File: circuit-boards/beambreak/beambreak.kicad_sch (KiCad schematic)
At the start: 12 parts, among them J1 POWER, J2 SENSOR, J3 RRIB, U1 H11L1SM

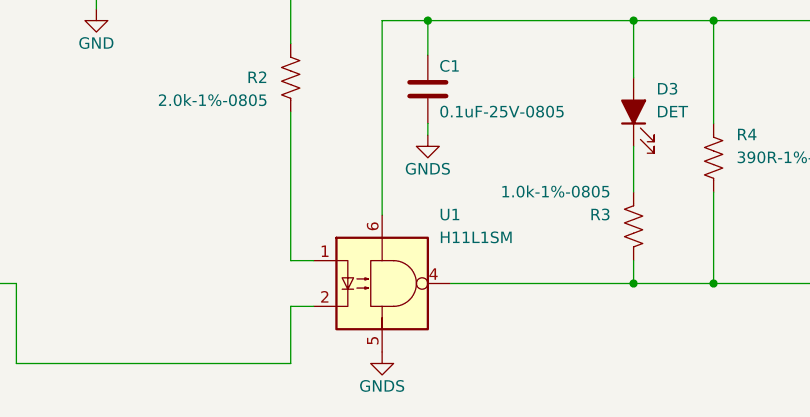
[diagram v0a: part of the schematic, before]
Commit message: Fixing bom and created gerbers for beam break board
Signed-off-by: Scott Berman <sgberman1@gmail.com>
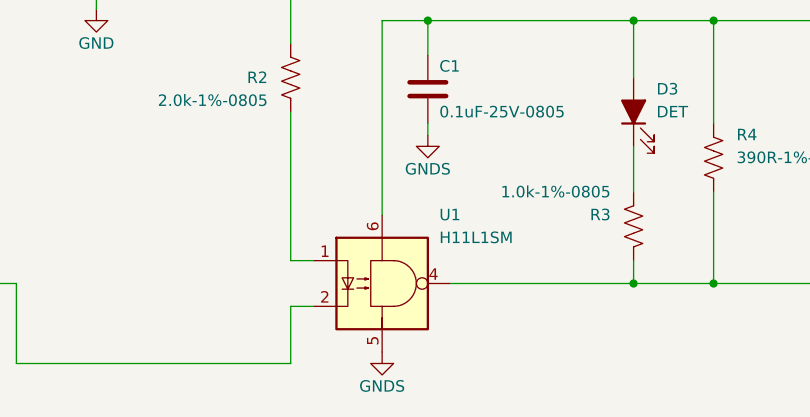
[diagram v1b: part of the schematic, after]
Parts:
- C1: DIST (none) -> Digikey; DIST P/N (none) -> 478-KGM21NR71E104KTCT-ND; MFG (none) -> KYOCERA AVX; MFG P/N (none) -> KGM21NR71E104KT
- D1, D3: DIST (none) -> Digikey; DIST P/N (none) -> 492-1945-1-ND; MFG (none) -> Bivar Inc.; MFG P/N (none) -> SM1206NPGC-IL
- D2: DIST (none) -> Digikey; DIST P/N (none) -> S1D-FDICT-ND
- J1: DIST (none) -> Digikey; DIST P/N (none) -> WM4164-ND
- J2: DIST (none) -> Digikey; DIST P/N (none) -> WM4166-ND
- J3: DIST (none) -> Digikey; DIST P/N (none) -> WM4165-ND
- R1: DIST (none) -> Digikey; DIST P/N (none) -> RNCP0805FTD2K00CT-ND
- R2: DIST (none) -> Digikey; DIST P/N (none) -> RNCP0805FTD2K00CT-ND; MFG (none) -> Stackpole Electronics; MFG P/N (none) -> RNCP0805FTD2K00
- R3: DIST (none) -> Digikey; DIST P/N (none) -> RNCP0805FTD1K00CT-ND
- R4: DIST (none) -> Digikey; DIST P/N (none) -> RMCF1206FT390RCT-ND
- U1: DIST (none) -> Digikey; DIST P/N (none) -> H11L1SM-ND
